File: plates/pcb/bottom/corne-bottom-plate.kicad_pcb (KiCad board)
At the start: 2 copper layers, 133.8 x 91.4 mm, 7 parts

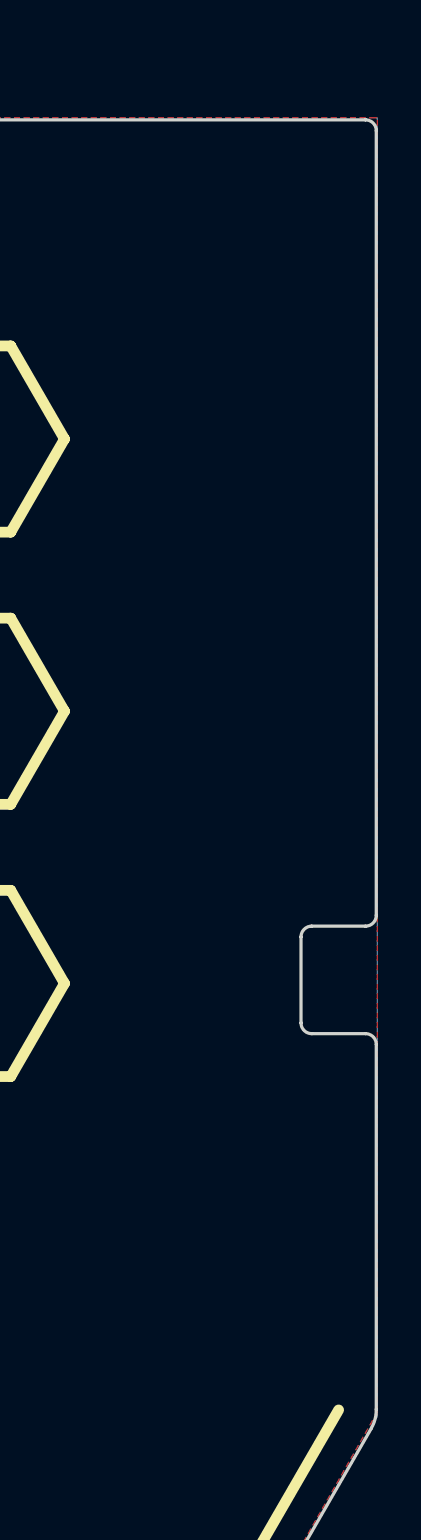
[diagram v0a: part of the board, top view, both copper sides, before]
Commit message: chocs are back, rerouting to allow removing the hole contact
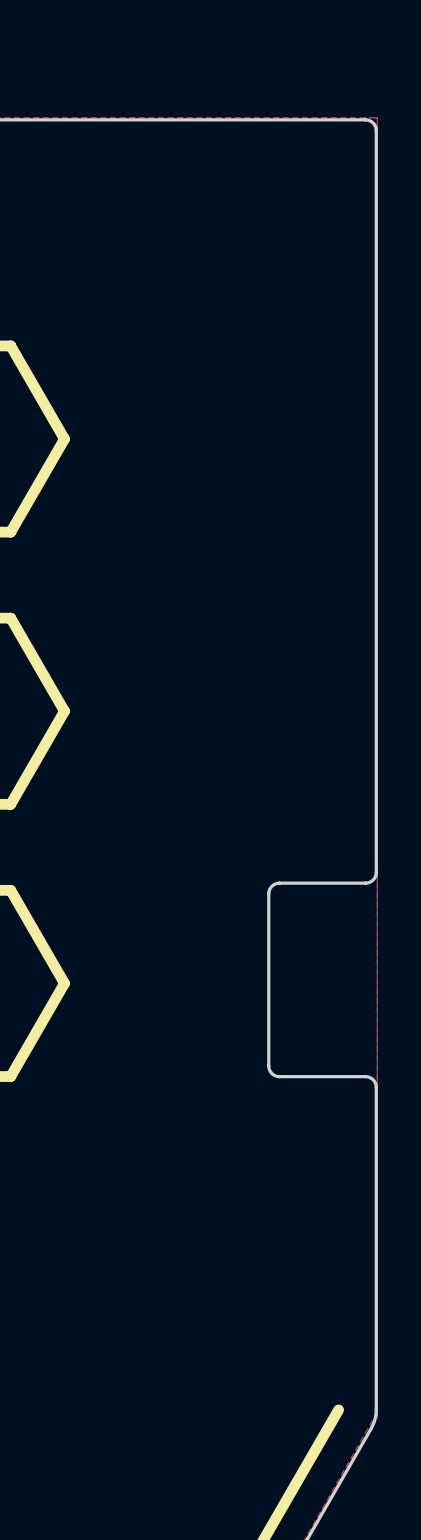
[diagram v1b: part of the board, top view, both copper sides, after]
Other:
- outline, holes or cut-outs redrawn
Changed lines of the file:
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@@
 	)
 	(gr_arc
-		(start 191.75 110.5)
-		(mid 191.396447 110.353553)
-		(end 191.25 110)
+		(start 190.25 112.5)
+		(mid 189.896447 112.353553)
+		(end 189.75 112)
 		(stroke
 			(width 0.15)
@@
 	)
 	(gr_arc
-		(start 191.25 106)
-		(mid 191.396447 105.646447)
-		(end 191.75 105.5)
+		(start 189.75 104)
+		(mid 189.896447 103.646447)
+		(end 190.25 103.5)
 		(stroke
 			(width 0.15)
@@
 	(gr_line
 		(start 194.750048 127.975)
-		(end 194.750048 111)
+		(end 194.75 113)
 		(stroke
 			(width 0.15)
@@
 	)
 	(gr_line
-		(start 191.75 105.5)
-		(end 194.25 105.5)
+		(start 190.25 103.5)
+		(end 194.25 103.5)
 		(stroke
 			(width 0.15)
@@
 	)
 	(gr_arc
-		(start 194.75 105)
-		(mid 194.603553 105.353553)
-		(end 194.25 105.5)
+		(start 194.75 103)
+		(mid 194.603553 103.353553)
+		(end 194.25 103.5)
 		(stroke
 			(width 0.15)
@@
 	)
 	(gr_line
-		(start 194.25 110.5)
-		(end 191.75 110.5)
+		(start 194.25 112.5)
+		(end 190.25 112.5)
 		(stroke
 			(width 0.15)
@@
 	)
 	(gr_arc
-		(start 194.25 110.5)
-		(mid 194.603553 110.646447)
-		(end 194.75 111)
+		(start 194.25 112.5)
+		(mid 194.603553 112.646447)
+		(end 194.75 113)
 		(stroke
 			(width 0.15)
@@
 	)
 	(gr_line
-		(start 194.75 105)
+		(start 194.75 103)
 		(end 194.75 68.5)
 		(stroke
@@
 	)
 	(gr_line
-		(start 191.25 110)
-		(end 191.25 106)
-		(stroke
-			(width 0.15)
+		(start 189.75 112)
+		(end 189.75 104)
+		(stroke
+			(width 0.15)
